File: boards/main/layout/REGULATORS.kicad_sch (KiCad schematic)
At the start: 30 parts, among them IC7 L6981N33DR, J1 B02B-PASK(LF)(SN), Q6 HSBB3072, SW4 MK-12D18-G040, U1 TPS611781RNWR, U3 CJA1117B-3.3

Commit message: 🏷️ Name the main board's module ports after their nets
A module's signal port now takes the name of the board net it carries (Fan_Enable, Wall_Sensor_0, Button), so its sheet pin and hierarchical label match the root's label: KiCad's ERC flagged each pair as similar_labels, names that differ only in case. The SPI buses and the Motor_*_Sense+/- nets, whose names are not identifiers, keep their port names. GND_BAT becomes a ground port of REGULATORS, so it reaches the root as a power symbol at the sheet pin instead of a dangling label. The netlist is unchanged: same nets, same names.
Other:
- moved on the sheet: C42, C43, C44, C45, C46, C47, C48, C49, C50, C51, C52, C53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

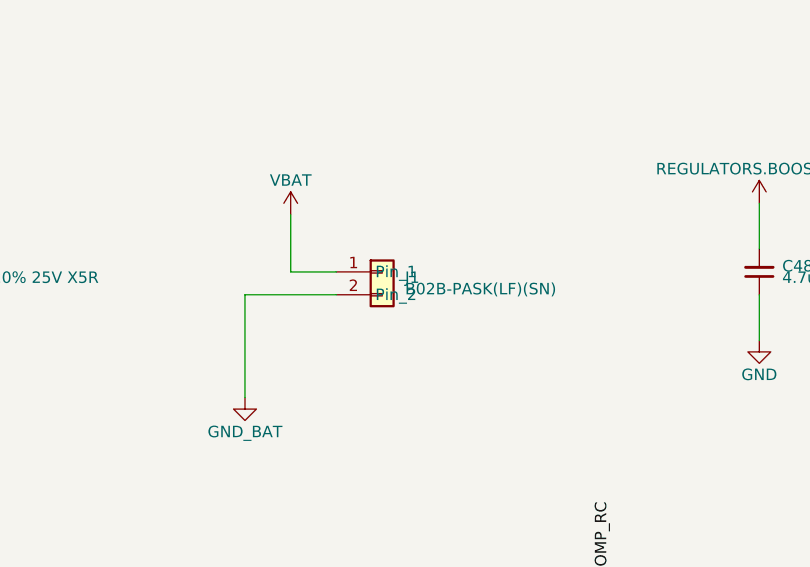
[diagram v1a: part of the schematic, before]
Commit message: ✨ Place the schematics from per-sheet placement files: the tool's fixes, the B02B pin names, docs, and the encoder, Bluetooth and DRIVERS placements for this revision
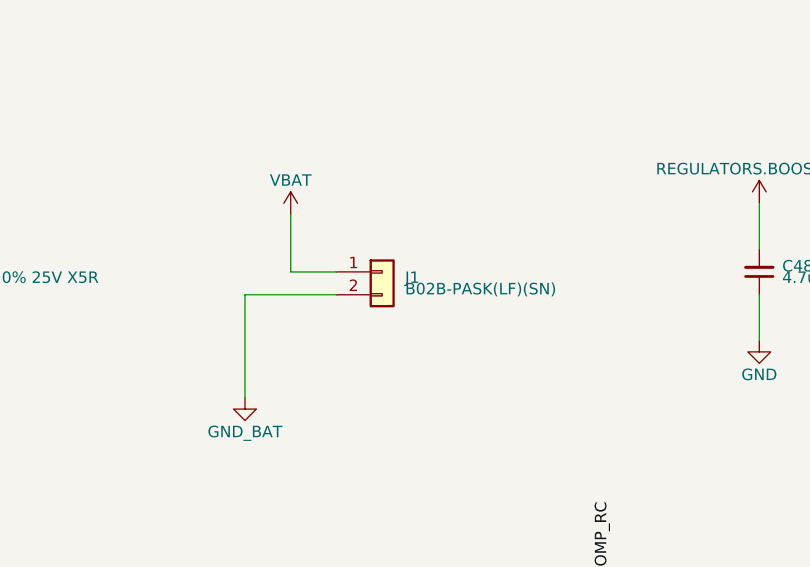
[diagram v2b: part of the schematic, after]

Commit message: 🎨 Place this revision's root, REGULATORS and SENSORS sheets; give the CJA1117B room for its pin names
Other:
- note added: "20 V boost: TPS611781 from VBAT for the L6205 bridges"
- note added: "3V3 buck: L6981N33 from VBAT"
- note added: "Battery input and switch: J1, SW4, low-side Q6"
- note added: "USB LDO: CJA1117B-3.3, +5V to 3V3"
- title: (none) -> Battery, regulators
- moved on the sheet: C42, C43, C44, C45, C46, C47, C48, C49, C50, C51, C52, C53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
